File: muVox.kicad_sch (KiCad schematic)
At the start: 57 parts

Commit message: Updated readme and pictures!
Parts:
- C1, C6, C7: value (none) -> 10uF; footprint (none) -> Capacitor_SMD:C_0805_2012Metric
- C2, C3: value (none) -> 10µF; footprint (none) -> Capacitor_SMD:C_0805_2012Metric
- C4: value (none) -> 10nF; footprint (none) -> Capacitor_SMD:C_0805_2012Metric
- C5: value (none) -> 100µF; footprint (none) -> Capacitor_SMD:C_Elec_5x5.4
- D1: value (none) -> STATUS; footprint (none) -> LED_SMD:LED_WS2812_PLCC6_5.0x5.0mm_P1.6mm
- D2, D4: value (none) -> 5V TVS; footprint (none) -> Diode_SMD:D_SOD-323
- D3: value (none) -> SS24FL; footprint (none) -> Diode_SMD:D_SOD-123F
- H1, H2, H3, H4: value (none) -> MountingHole_Pad; footprint (none) -> Lib:MountingHole_PSUDO_M4
- J1: value (none) -> STEMMA QT; footprint (none) -> Connector_JST:JST_SH_SM04B-SRSS-TB_1x04-1MP_P1.00mm_Horizontal
- J2: value (none) -> JTAG_EXTRA; footprint (none) -> Connector_IDC:IDC-Header_2x06_P2.54mm_Vertical
- J3: value (none) -> Programmer; footprint (none) -> Connector_PinHeader_2.54mm:PinHeader_1x06_P2.54mm_Vertical
- J4: value (none) -> Alt.DC; footprint (none) -> Connector_JST:JST_VH_B2PS-VH_1x02_P3.96mm_Horizontal
- J5: value (none) -> DC IN; footprint (none) -> Connector_BarrelJack:BarrelJack_CUI_PJ-063AH_Horizontal
- JP1: value (none) -> Jumper_2_Open; footprint (none) -> Jumper:SolderJumper-2_P1.3mm_Open_RoundedPad1.0x1.5mm
- JP2: value (none) -> Jumper_2_Bridged; footprint (none) -> Jumper:SolderJumper-2_P1.3mm_Bridged_RoundedPad1.0x1.5mm
- L1: value (none) -> 47µH; footprint (none) -> Inductor_SMD:L_10.4x10.4_H4.8
- R1, R10, R2, R9: value (none) -> 4.7KΩ; footprint (none) -> Resistor_SMD:R_0603_1608Metric
- R11: value (none) -> 3.2KΩ; footprint (none) -> Resistor_SMD:R_0603_1608Metric
- R12, R15, R16, R17, R6, R7: value (none) -> 10KΩ; footprint (none) -> Resistor_SMD:R_0603_1608Metric
- R13: value (none) -> 650KΩ; footprint (none) -> Resistor_SMD:R_0603_1608Metric
- R14: value (none) -> 100KΩ; footprint (none) -> Resistor_SMD:R_0603_1608Metric
- R3, R4, R5, R8: value (none) -> 2KΩ; footprint (none) -> Resistor_SMD:R_0603_1608Metric
- SW1: value (none) -> EG1206A; footprint (none) -> Lib:SLIDE-SWITCH
- TP1, TP10, TP11, TP12, TP13, TP2, TP3, TP4, TP5, TP6, TP7, TP8, TP9: value (none) -> TestPoint_Small; footprint (none) -> TestPoint:TestPoint_Pad_D1.5mm
- U1: value (none) -> TPS5430DDA; footprint (none) -> Package_SO:TI_SO-PowerPAD-8_ThermalVias
- U2: value (none) -> ZD24C08AE1; footprint (none) -> Package_TO_SOT_SMD:SOT-23-5
- U3: value (none) -> XC6220B331MR; footprint (none) -> Package_TO_SOT_SMD:SOT-23-5
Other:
- sheet DC Protection: file MEYERS_DC.kicad_sch -> DC_protection.kicad_sch
- note added: "0.9"
- note added: "3v3 LDO"
- note added: "MERUS AMPLIFIER"
- note removed: "0.7"
- note removed: "3v3"
- note removed: "AMPLIFIER"
- moved on the sheet: D1, D2, D4, H1, H2, H3, H4, R10, R13, R14, R3, R4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

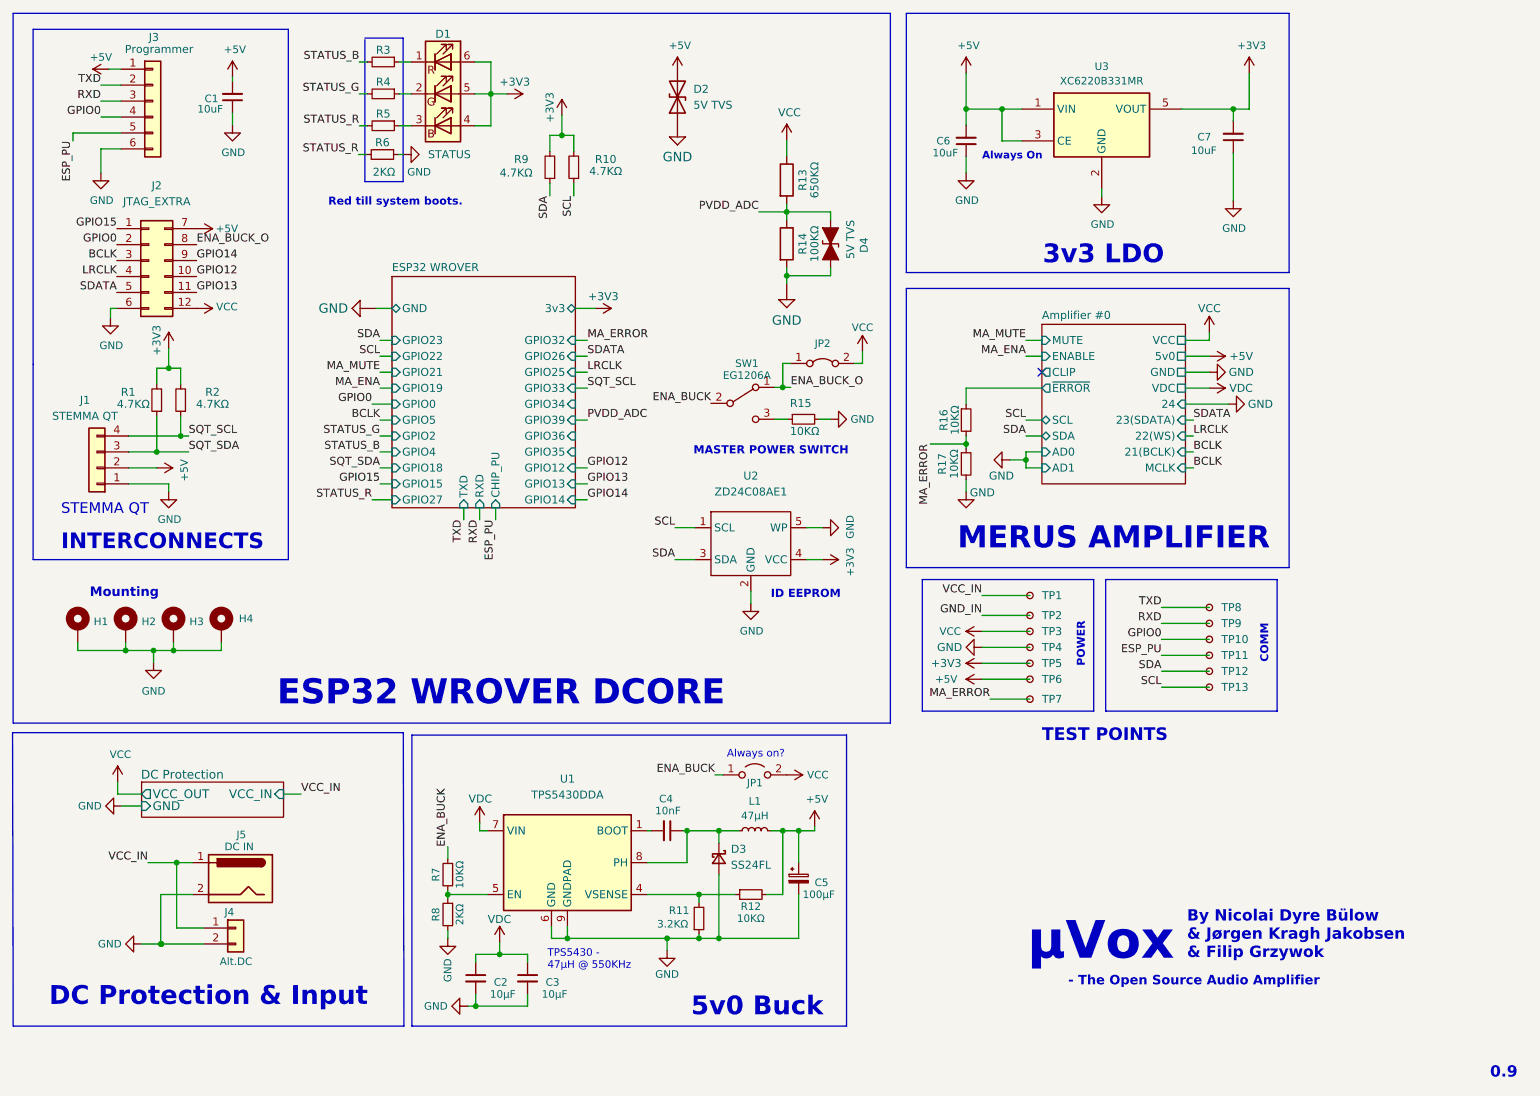
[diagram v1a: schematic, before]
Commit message: Redid symbol value and footprints for DC_Prot. Dont relink sub-schematics i guess..
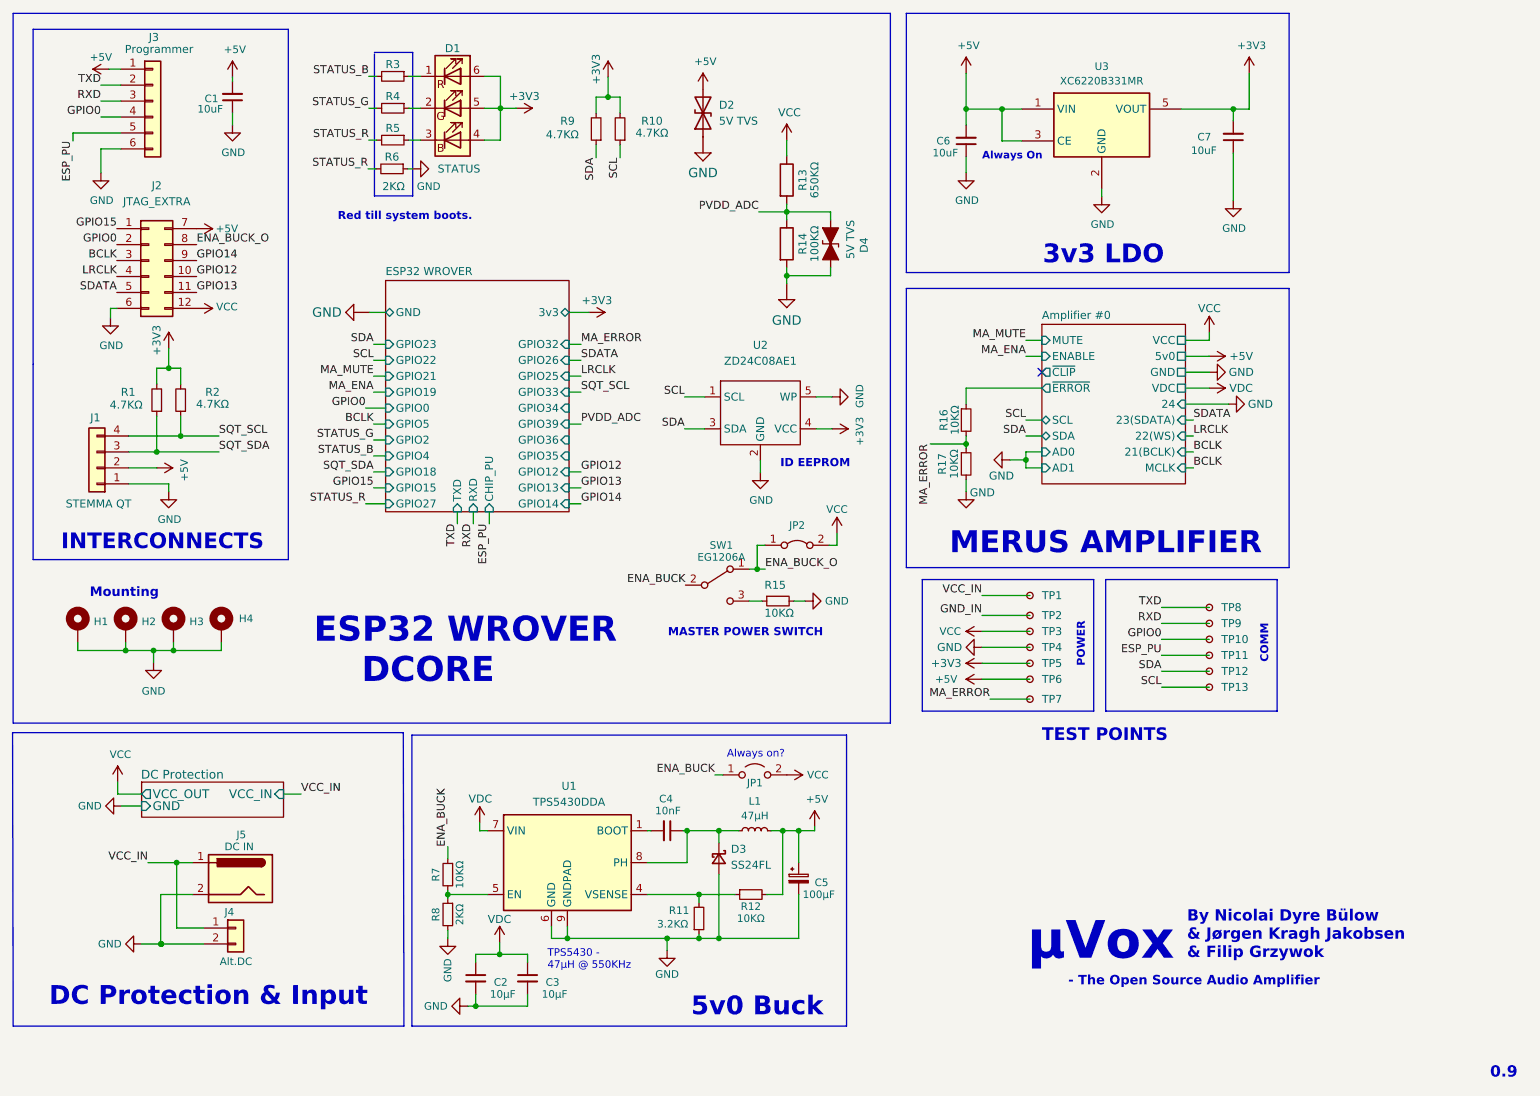
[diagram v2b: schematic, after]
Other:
- sheet Amplifier #0 ports: added ~{CLIP}; removed CLIP
- note removed: "STEMMA QT"
- moved on the sheet: D1, D2, JP2, R10, R15, R3, R4, R5, R6, R9, SW1, U2

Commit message: Exported updated gerbers
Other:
- moved on the sheet: C1, C2, C3, C4, C5, C6, C7, D1, D2, D3, D4, H1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
